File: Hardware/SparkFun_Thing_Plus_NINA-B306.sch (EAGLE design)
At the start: 80 parts, among them J1 USB-C, J2 THING_PLUS_LOGICAL, J3 CONN_03X2_NO4, J4 MICRO-SDFRICTION, J6 QWIIC_RA, Q1 20V/4.2A/52mΩ/1.4W, Q3 20V/4.2A/52mΩ/1.4W, U1 ESD Diode, U2 U-BLOX_NINA_B306, U3 XC6222B331MR-G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

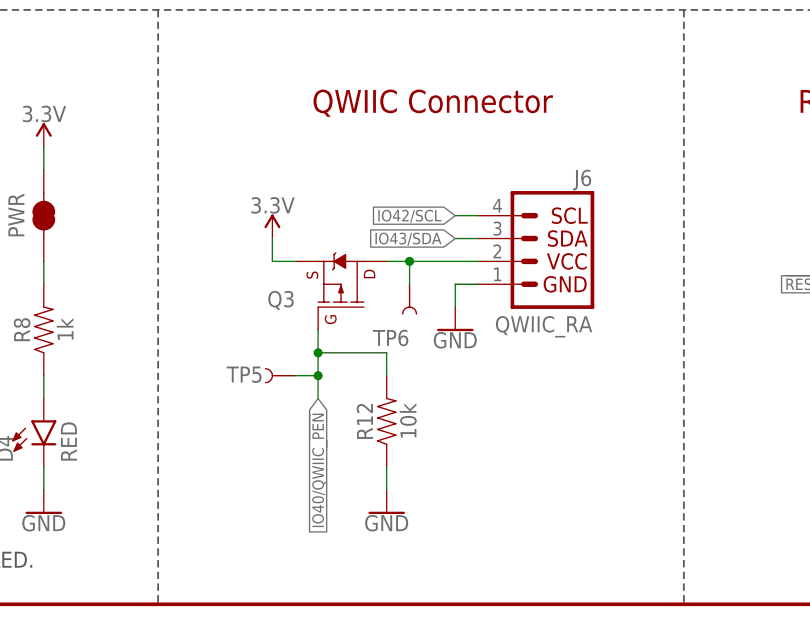
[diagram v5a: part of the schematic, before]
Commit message: Added Layer numbers
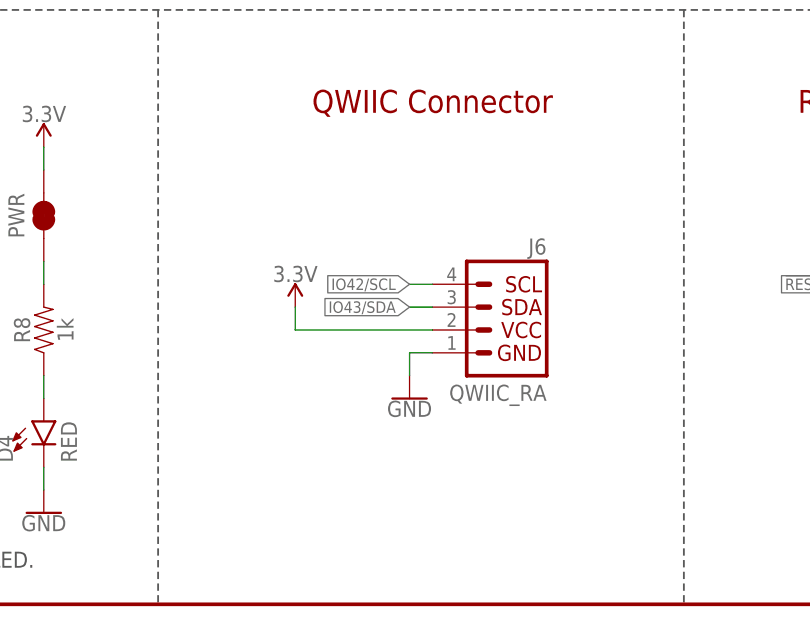
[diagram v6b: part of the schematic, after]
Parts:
- removed Q3: 20V/4.2A/52mΩ/1.4W, SparkFun-DiscreteSemi:MOSFET_PCH-DMG2305UX-7
- removed R12: 10k, SparkFun-Resistors:10KOHM-0402T-1/16W-1%
- removed TP5, TP6: TEST-POINT3X5, SparkFun-Connectors:TEST-POINT3X5
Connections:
- removed net 3V3_QWIIC: J6.2, Q3.D, TP6.1
- net 3.3V: now also J6.2; no longer Q3.S
- net GND: no longer R12.1
- net IO40/QWIIC_!PEN!: no longer Q3.G, R12.2, TP5.1
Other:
- moved on the sheet: J6
